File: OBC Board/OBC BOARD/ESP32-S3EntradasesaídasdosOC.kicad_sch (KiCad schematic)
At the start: 2 parts, among them J3 Conn_01x22_Socket, J4 Conn_01x22_Socket

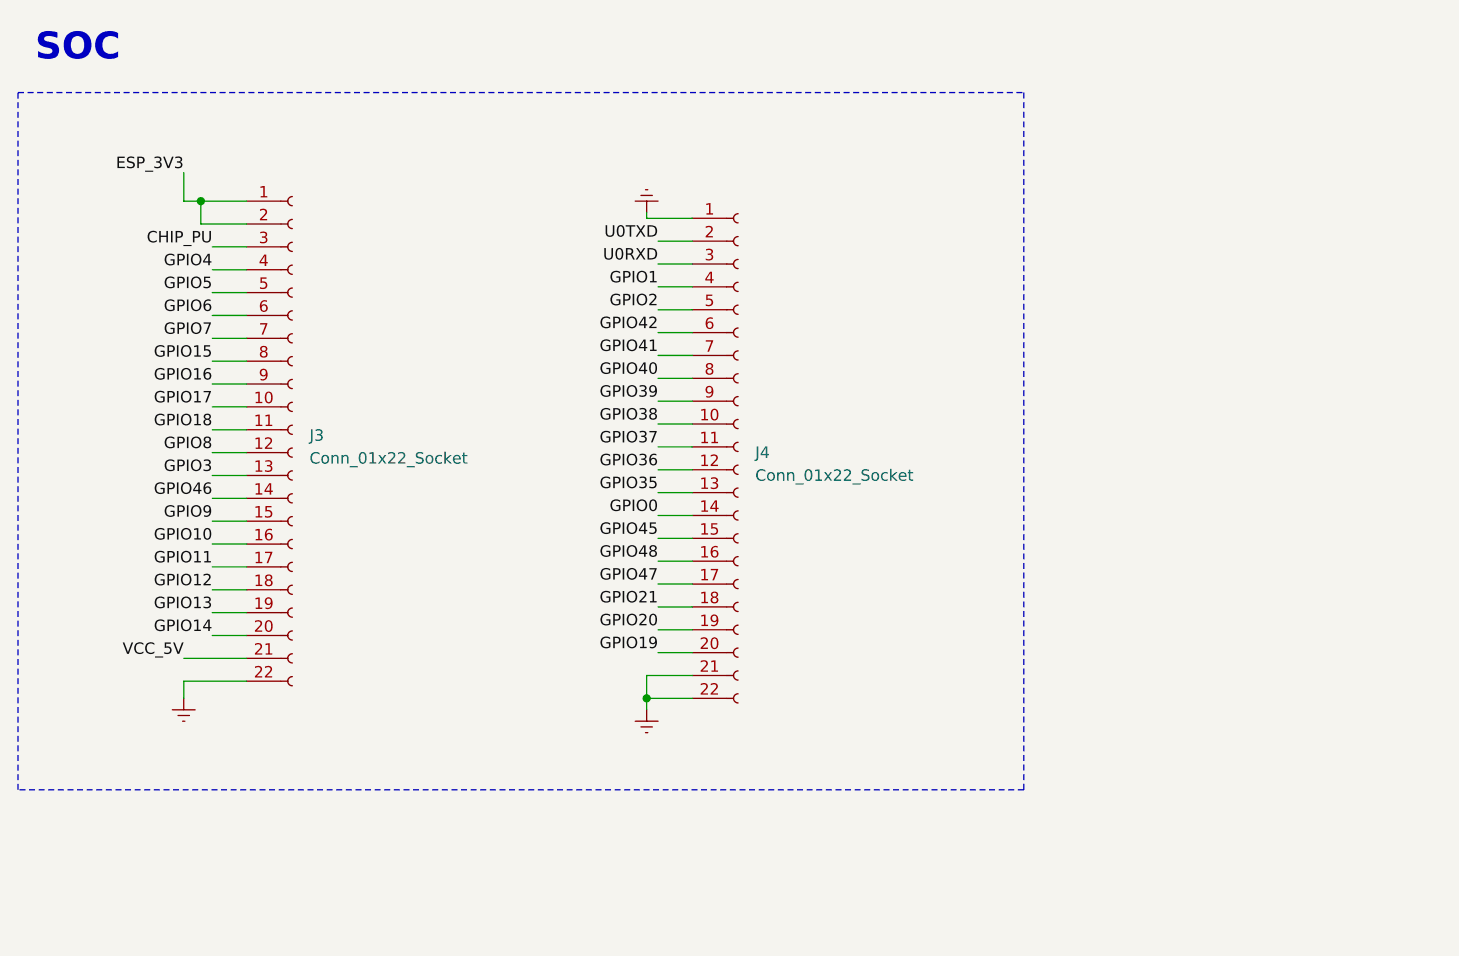
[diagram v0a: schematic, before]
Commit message: Realização do diagrama de blocos, test points, padronização e mudança dos caminhos das bibliotecas de footprints e simbolos
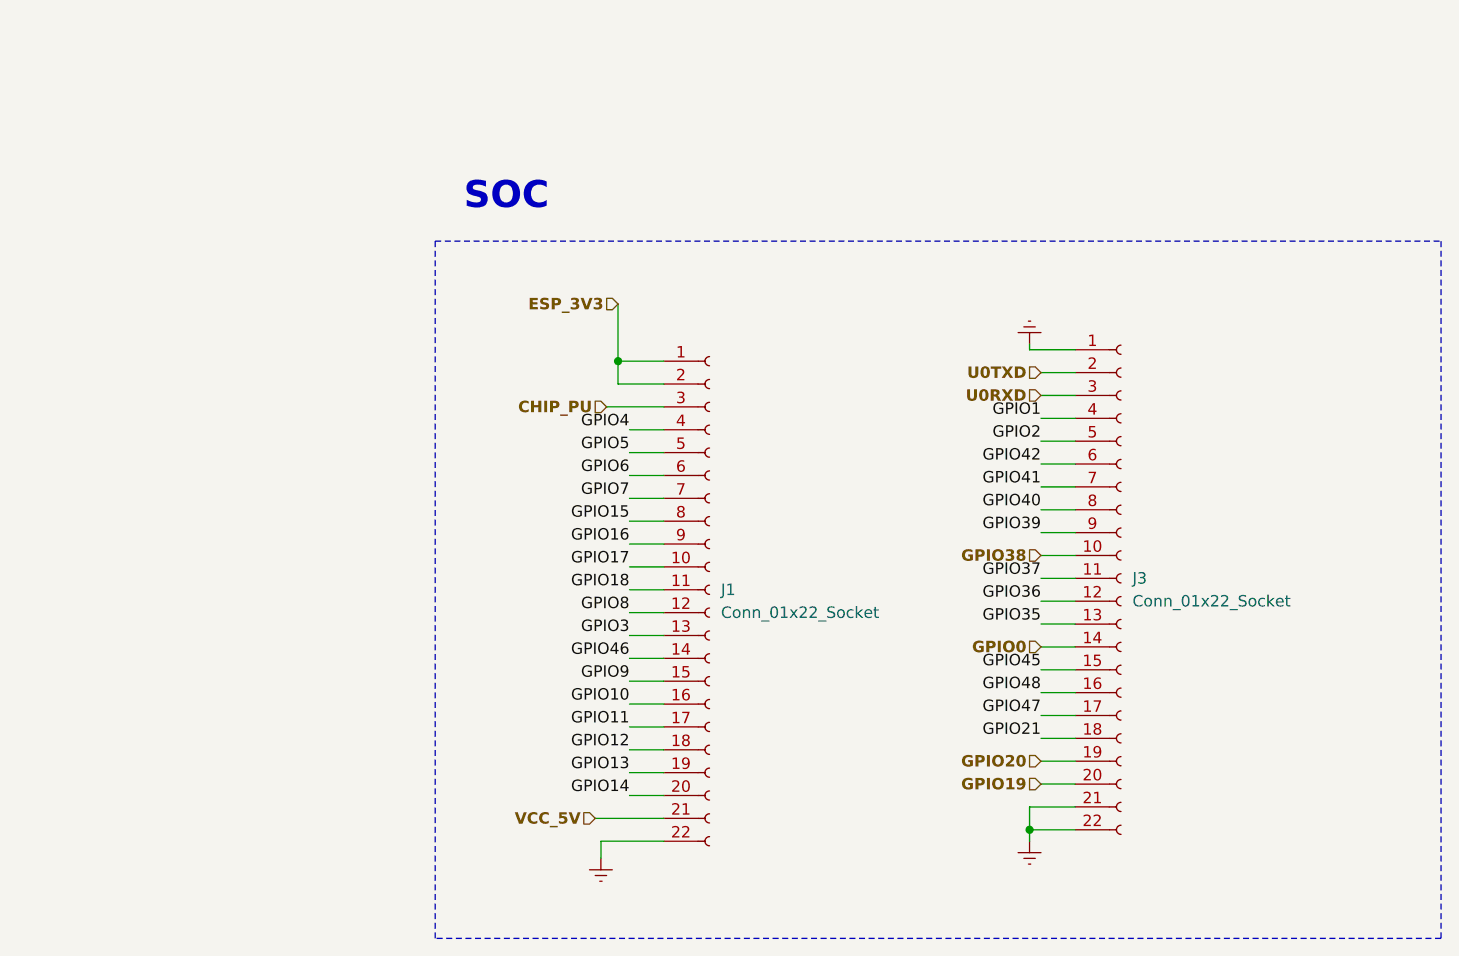
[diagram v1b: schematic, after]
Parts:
- J1: renamed from J3; footprint (none) -> Connector_PinSocket_2.54mm:PinSocket_1x22_P2.54mm_Vertical
- J3: renamed from J4; footprint (none) -> Connector_PinSocket_2.54mm:PinSocket_1x22_P2.54mm_Vertical
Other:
- title: ICARUS-2 OBCH -> ICARUS-2 OBDH
- moved on the sheet: J1, J3
